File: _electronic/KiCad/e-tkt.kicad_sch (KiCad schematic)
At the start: 1 part

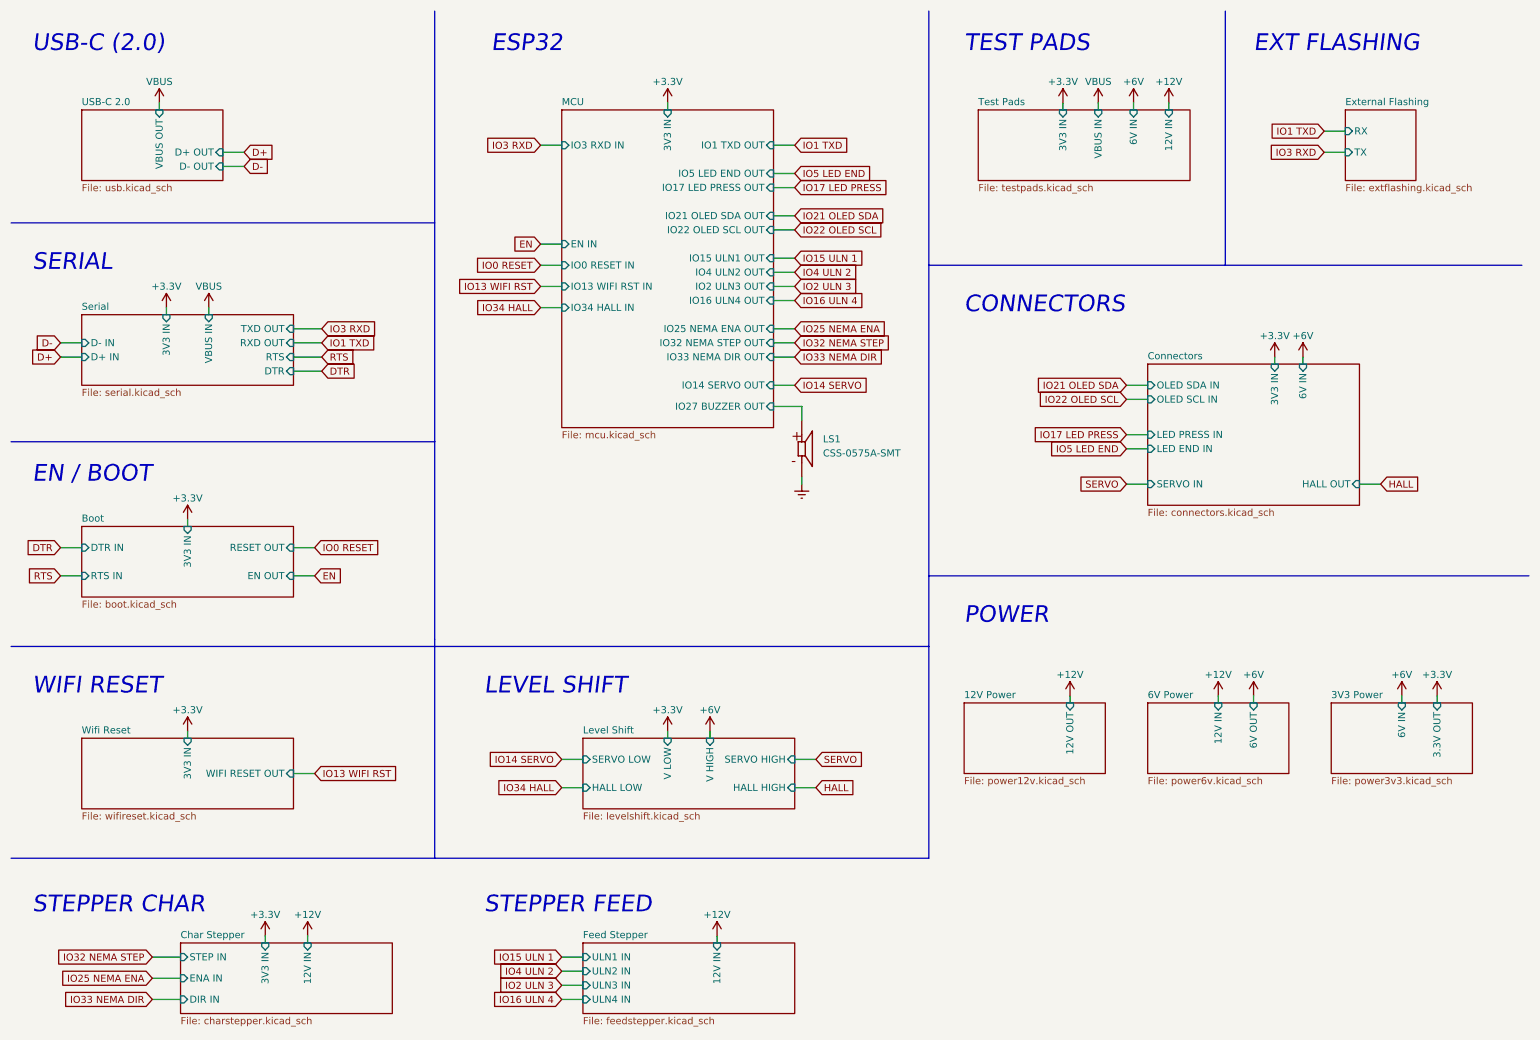
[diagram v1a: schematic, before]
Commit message: 6v and power latch backup
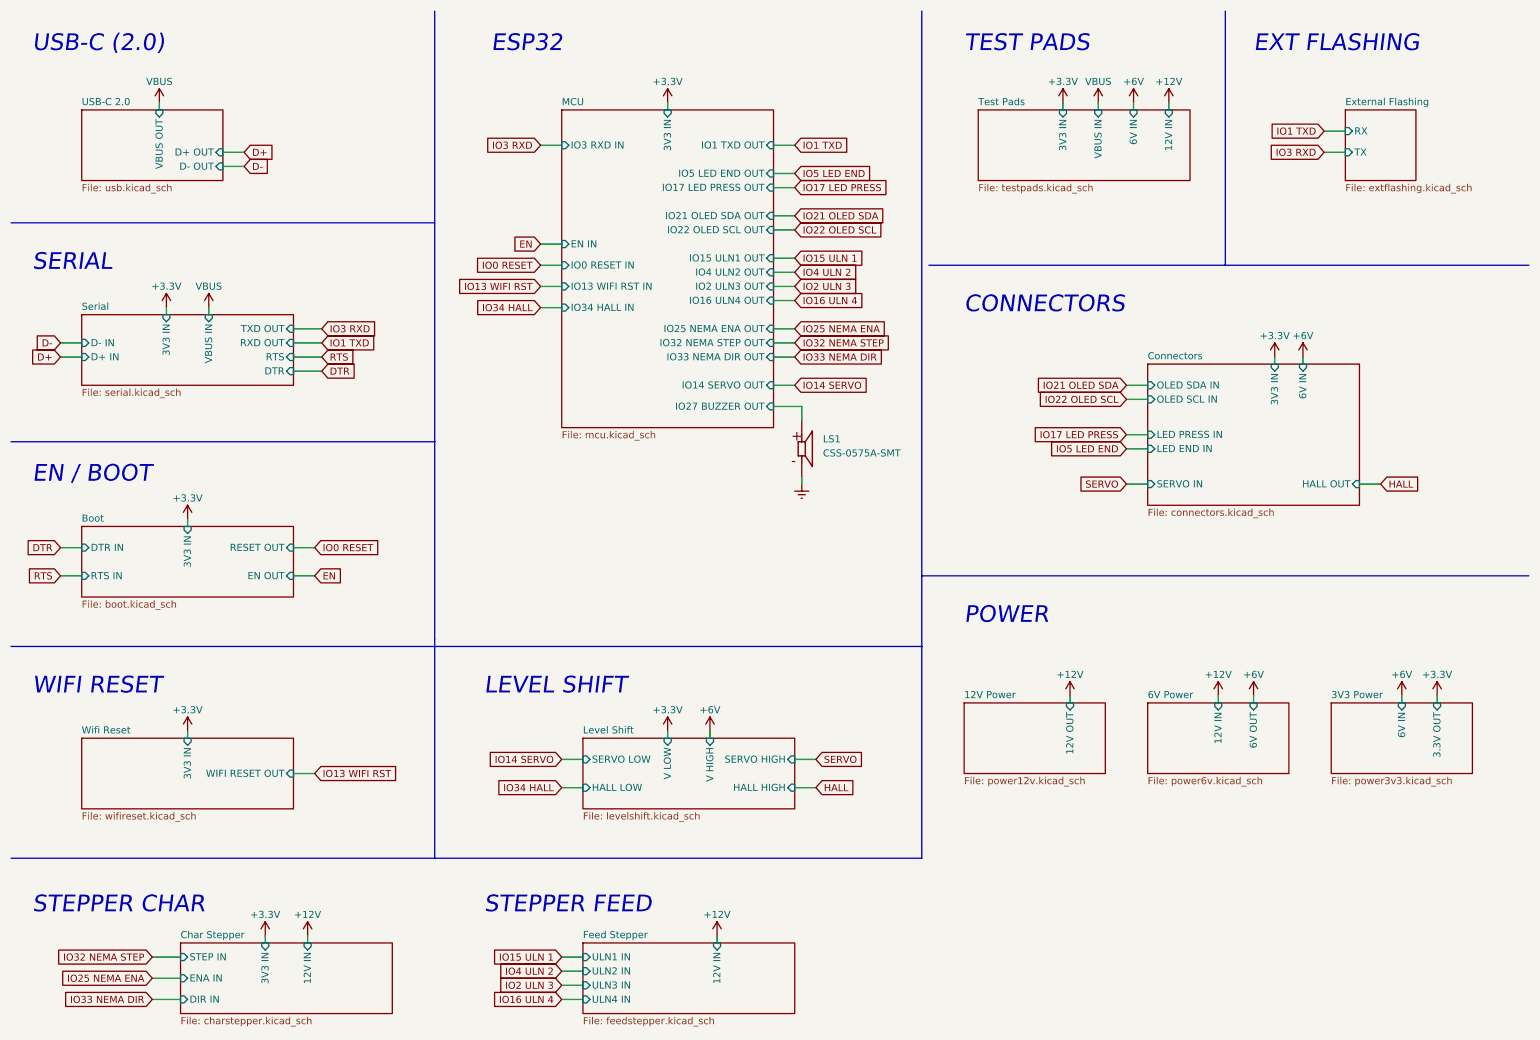
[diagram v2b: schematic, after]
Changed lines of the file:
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@@
     (stroke (width 0) (type default) (color 0 0 0 0))
   )
-  (polyline (pts (xy 12.7 127) (xy 177.8 127))
+  (polyline (pts (xy 12.7 127) (xy 176.53 127))
     (stroke (width 0) (type default) (color 0 0 0 0))
   )
@@
     (stroke (width 0) (type default) (color 0 0 0 0))
   )
-  (polyline (pts (xy 177.8 114.3) (xy 285.75 114.3))
+  (polyline (pts (xy 176.53 114.3) (xy 285.75 114.3))
     (stroke (width 0) (type default) (color 0 0 0 0))
   )
@@
     (stroke (width 0) (type default) (color 0 0 0 0))
   )
-  (polyline (pts (xy 177.8 12.7) (xy 177.8 127))
+  (polyline (pts (xy 176.53 12.7) (xy 176.53 127))
     (stroke (width 0) (type default) (color 0 0 0 0))
   )
@@
     (stroke (width 0) (type default) (color 0 0 0 0))
   )
-  (polyline (pts (xy 12.7 165.1) (xy 177.8 165.1))
+  (polyline (pts (xy 12.7 165.1) (xy 176.53 165.1))
     (stroke (width 0) (type default) (color 0 0 0 0))
   )
@@
     (stroke (width 0) (type default) (color 0 0 0 0))
   )
-  (polyline (pts (xy 177.8 58.42) (xy 284.48 58.42))
+  (polyline (pts (xy 177.8 58.42) (xy 285.75 58.42))
     (stroke (width 0) (type default) (color 0 0 0 0))
   )
@@
     (stroke (width 0) (type default) (color 0 0 0 0))
   )
-  (polyline (pts (xy 177.8 165.1) (xy 177.8 127))
+  (polyline (pts (xy 176.53 165.1) (xy 176.53 127))
     (stroke (width 0) (type default) (color 0 0 0 0))
   )
@@
       (reference "#PWR0138") (unit 1) (value "GNDREF") (footprint "")
     )
+    (path "/9f001140-4433-4565-aea0-4a74283269e6/35b90b2b-adaa-49f9-9780-9f3269bd7b9b"
+      (reference "#PWR0139") (unit 1) (value "~") (footprint "")
+    )
     (path "/077b7f8a-3b82-46ad-b55a-a178b69955aa"
       (reference "#PWR0140") (unit 1) (value "+3.3V") (footprint "")
@@
       (reference "C_POW_BST1") (unit 1) (value "0.1uF 50V") (footprint "Capacitor_SMD:C_0603_1608Metric_Pad1.08x0.95mm_HandSolder")
     )
+    (path "/9f001140-4433-4565-aea0-4a74283269e6/4c138899-24f6-4346-84a3-079ab48bfd51"
+      (reference "C_POW_BST?") (unit 1) (value "0.1uF 50V") (footprint "Capacitor_SMD:C_0603_1608Metric_Pad1.08x0.95mm_HandSolder")
+    )
+    (path "/9f001140-4433-4565-aea0-4a74283269e6/522178cd-7448-4933-9e06-766ff3399aa0"
+      (reference "C_POW_BST?") (unit 1) (value "0.33uF 50V") (footprint "Capacitor_SMD:C_0603_1608Metric_Pad1.08x0.95mm_HandSolder")
+    )
     (path "/9f001140-4433-4565-aea0-4a74283269e6/2650722c-9362-4b86-aae3-128504da3aed"
       (reference "C_POW_IN1") (unit 1) (value "10uF 25V") (footprint "Capacitor_SMD:C_1210_3225Metric_Pad1.33x2.70mm_HandSolder")
@@
       (reference "H6") (unit 1) (value "M3") (footprint "MountingHole:MountingHole_3.2mm_M3_Pad_Via")
     )
+    (path "/ab008ac4-72ad-4687-86ad-8fa342b57840/e39b4501-907d-425d-8868-070c1c163e4b"
+      (reference "JP1") (unit 1) (value "SolderJumper_2_Open") (footprint "Jumper:SolderJumper-2_P1.3mm_Open_Pad1.0x1.5mm")
+    )
+    (path "/ab008ac4-72ad-4687-86ad-8fa342b57840/2a6563ec-0124-4af8-ac6b-cc7e5decc9de"
+      (reference "JP2") (unit 1) (value "SolderJumper_2_Open") (footprint "Jumper:SolderJumper-2_P1.3mm_Open_Pad1.0x1.5mm")
+    )
     (path "/500f785f-7d37-4530-93ef-964340f250e0/759808a4-0a98-4db1-b6cd-14f38dcf5202"
       (reference "JP_SER1") (unit 1) (value "Bridged") (footprint "Jumper:SolderJumper-2_P1.3mm_Bridged2Bar_Pad1.0x1.5mm")
@@
       (reference "J_28byj-48-12v_1") (unit 1) (value "Conn_01x05_Male") (footprint "Connector_PinHeader_2.54mm:PinHeader_1x05_P2.54mm_Vertical")
     )
+    (path "/9f001140-4433-4565-aea0-4a74283269e6/5787ec46-6505-49d4-a0a4-ef8cba819874"
+      (reference "J_B_6v_1") (unit 1) (value "TestPoint") (footprint "TestPoint:TestPoint_Pad_D1.5mm")
+    )
+    (path "/9f001140-4433-4565-aea0-4a74283269e6/141af5fb-8652-4a21-a0a8-bcbc7640f184"
+      (reference "J_B_12v_1") (unit 1) (value "TestPoint") (footprint "TestPoint:TestPoint_Pad_D1.5mm")
+    )
+    (path "/9f001140-4433-4565-aea0-4a74283269e6/21e11354-cb62-4cc5-918e-6586b07cda59"
+      (reference "J_B_GND_1") (unit 1) (value "TestPoint") (footprint "TestPoint:TestPoint_Pad_D1.5mm")
+    )
     (path "/6b620b21-f9f4-45f9-ae29-09e80b0a55df/5fddb882-70ad-4f15-bda9-3a4789178dfd"
       (reference "J_EXT1") (unit 1) (value "Conn_01x03_Male") (footprint "Connector_PinHeader_2.54mm:PinHeader_1x03_P2.54mm_Horizontal")
@@
     )
     (path "/ab008ac4-72ad-4687-86ad-8fa342b57840/31888d71-a910-43e3-86b4-828fb2c3a7da"
-      (reference "Q_POW1") (unit 1) (value "IRLML6302TRPBF") (footprint "Package_TO_SOT_SMD:SOT-23")
+      (reference "Q_POW1") (unit 1) (value "SQ2351ES-T1_GE3") (footprint "Package_TO_SOT_SMD:SOT-23")
     )
     (path "/ab008ac4-72ad-4687-86ad-8fa342b57840/f562e358-c278-4a32-864f-f165e5e1d305"
